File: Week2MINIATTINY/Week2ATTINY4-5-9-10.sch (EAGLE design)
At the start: 16 parts

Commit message: schemematic updates
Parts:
- added R5: (no value), rcl:R-EU_R0603
- JP1: value M021X02_NO_SILK -> RESET_PULLUP_ENABLE
- JP2: value M021X02_NO_SILK -> EXTERNAL_CLK_ENABLE
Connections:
- new net IO1: JP6.2, R1.2
- new net IO2: JP6.3, R2.2
- new net IO3: JP6.4, R3.2
- new net IO4: JP6.5, R4.2
- new net RESET_PULLUP: JP1.2, R5.1
- net GND: now also C1.2, C2.2, C3.2, C4.2, JP6.6
- net PB0: now also R1.1
- net PB1: now also R2.1
- net PB2: now also R3.1
- net PB3/_RESET: now also JP1.1, R4.1
- net VCC: now also C1.1, C2.1, C3.1, C4.1, JP6.1, R5.2
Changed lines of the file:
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@@
 <part name="GND1" library="supply1" library_urn="urn:adsk.eagle:library:371" deviceset="GND" device=""/>
 <part name="P+1" library="supply1" library_urn="urn:adsk.eagle:library:371" deviceset="VCC" device=""/>
-<part name="JP1" library="SparkFun-Connectors" deviceset="M02" device="1X02_NO_SILK"/>
-<part name="JP2" library="SparkFun-Connectors" deviceset="M02" device="1X02_NO_SILK"/>
+<part name="JP1" library="SparkFun-Connectors" deviceset="M02" device="1X02_NO_SILK" value="RESET_PULLUP_ENABLE"/>
+<part name="JP2" library="SparkFun-Connectors" deviceset="M02" device="1X02_NO_SILK" value="EXTERNAL_CLK_ENABLE"/>
 <part name="JP3" library="SparkFun-Connectors" deviceset="M02" device="1X02_NO_SILK"/>
 <part name="JP4" library="SparkFun-Connectors" deviceset="M02" device="1X02_NO_SILK"/>
@@
 <part name="C4" library="rcl" library_urn="urn:adsk.eagle:library:334" deviceset="C-EU" device="C0603K" package3d_urn="urn:adsk.eagle:package:23680/2"/>
 <part name="R4" library="rcl" library_urn="urn:adsk.eagle:library:334" deviceset="R-EU_" device="R0603" package3d_urn="urn:adsk.eagle:package:23555/2"/>
+<part name="GND2" library="supply1" library_urn="urn:adsk.eagle:library:371" deviceset="GND" device=""/>
+<part name="GND3" library="supply1" library_urn="urn:adsk.eagle:library:371" deviceset="GND" device=""/>
+<part name="GND4" library="supply1" library_urn="urn:adsk.eagle:library:371" deviceset="GND" device=""/>
+<part name="GND5" library="supply1" library_urn="urn:adsk.eagle:library:371" deviceset="GND" device=""/>
+<part name="P+2" library="supply1" library_urn="urn:adsk.eagle:library:371" deviceset="VCC" device=""/>
+<part name="P+3" library="supply1" library_urn="urn:adsk.eagle:library:371" deviceset="VCC" device=""/>
+<part name="P+4" library="supply1" library_urn="urn:adsk.eagle:library:371" deviceset="VCC" device=""/>
+<part name="P+5" library="supply1" library_urn="urn:adsk.eagle:library:371" deviceset="VCC" device=""/>
+<part name="R5" library="rcl" library_urn="urn:adsk.eagle:library:334" deviceset="R-EU_" device="R0603" package3d_urn="urn:adsk.eagle:package:23555/2"/>
+<part name="P+6" library="supply1" library_urn="urn:adsk.eagle:library:371" deviceset="VCC" device=""/>
+<part name="P+7" library="supply1" library_urn="urn:adsk.eagle:library:371" deviceset="VCC" device=""/>
+<part name="GND6" library="supply1" library_urn="urn:adsk.eagle:library:371" deviceset="GND" device=""/>
 </parts>
 <sheets>
@@
 <instance part="C4" gate="G$1" x="127" y="38.1"/>
 <instance part="R4" gate="G$1" x="76.2" y="20.32"/>
+<instance part="GND2" gate="1" x="101.6" y="22.86"/>
+<instance part="GND3" gate="1" x="111.76" y="22.86"/>
+<instance part="GND4" gate="1" x="119.38" y="22.86"/>
+<instance part="GND5" gate="1" x="127" y="22.86"/>
+<instance part="P+2" gate="VCC" x="101.6" y="53.34"/>
+<instance part="P+3" gate="VCC" x="111.76" y="53.34"/>
+<instance part="P+4" gate="VCC" x="119.38" y="53.34"/>
+<instance part="P+5" gate="VCC" x="127" y="53.34"/>
+<instance part="R5" gate="G$1" x="71.12" y="63.5" rot="R90"/>
+<instance part="P+6" gate="VCC" x="71.12" y="78.74"/>
+<instance part="P+7" gate="VCC" x="25.4" y="86.36"/>
+<instance part="GND6" gate="1" x="25.4" y="55.88"/>
 </instances>
 <busses>
@@
 <label x="292.1" y="175.26" size="1.778" layer="95"/>
 </segment>
+<segment>
+<pinref part="R4" gate="G$1" pin="1"/>
+<wire x1="71.12" y1="20.32" x2="60.96" y2="20.32" width="0.1524" layer="91"/>
+<label x="58.42" y="20.32" size="1.778" layer="95"/>
+</segment>
+<segment>
+<pinref part="JP1" gate="G$1" pin="1"/>
+<wire x1="165.1" y1="88.9" x2="147.32" y2="88.9" width="0.1524" layer="91"/>
+<label x="147.32" y="88.9" size="1.778" layer="95"/>
+</segment>
 </net>
 <net name="PB2" class="0">
@@
 <label x="292.1" y="170.18" size="1.778" layer="95"/>
 </segment>
+<segment>
+<pinref part="R3" gate="G$1" pin="1"/>
+<wire x1="71.12" y1="27.94" x2="60.96" y2="27.94" width="0.1524" layer="91"/>
+<label x="60.96" y="27.94" size="1.778" layer="95"/>
+</segment>
 </net>
 <net name="PB0" class="0">
@@
 <label x="241.3" y="170.18" size="1.778" layer="95"/>
 </segment>
+<segment>
+<pinref part="R1" gate="G$1" pin="1"/>
+<wire x1="71.12" y1="43.18" x2="60.96" y2="43.18" width="0.1524" layer="91"/>
+<label x="60.96" y="43.18" size="1.778" layer="95"/>
+</segment>
 </net>
 <net name="PB1" class="0">
@@
 <wire x1="251.46" y1="165.1" x2="241.3" y2="165.1" width="0.1524" layer="91"/>
 <label x="241.3" y="165.1" size="1.778" layer="95"/>
+</segment>
+<segment>
+<pinref part="R2" gate="G$1" pin="1"/>
+<wire x1="71.12" y1="35.56" x2="60.96" y2="35.56" width="0.1524" layer="91"/>
+<label x="60.96" y="35.56" size="1.778" layer="95"/>
 </segment>
 </net>
@@
 <pinref part="GND1" gate="1" pin="GND"/>
 </segment>
+<segment>
+<pinref part="C1" gate="G$1" pin="2"/>
+<wire x1="101.6" y1="33.02" x2="101.6" y2="25.4" width="0.1524" layer="91"/>
+<pinref part="GND2" gate="1" pin="GND"/>
+</segment>
+<segment>
+<pinref part="C2" gate="G$1" pin="2"/>
+<wire x1="111.76" y1="33.02" x2="111.76" y2="25.4" width="0.1524" layer="91"/>
+<pinref part="GND3" gate="1" pin="GND"/>
+</segment>
+<segment>
+<pinref part="C3" gate="G$1" pin="2"/>
+<wire x1="119.38" y1="33.02" x2="119.38" y2="25.4" width="0.1524" layer="91"/>
+<pinref part="GND4" gate="1" pin="GND"/>
+</segment>
+<segment>
+<pinref part="C4" gate="G$1" pin="2"/>
+<wire x1="127" y1="33.02" x2="127" y2="25.4" width="0.1524" layer="91"/>
+<pinref part="GND5" gate="1" pin="GND"/>
+</segment>
+<segment>
+<pinref part="JP6" gate="G$1" pin="6"/>
+<wire x1="35.56" y1="63.5" x2="25.4" y2="63.5" width="0.1524" layer="91"/>
+<wire x1="25.4" y1="63.5" x2="25.4" y2="58.42" width="0.1524" layer="91"/>
+<pinref part="GND6" gate="1" pin="GND"/>
+</segment>
 </net>
 <net name="VCC" class="0">
@@
 <pinref part="P+1" gate="VCC" pin="VCC"/>
 </segment>
-</net>
+<segment>
+<pinref part="C1" gate="G$1" pin="1"/>
+<wire x1="101.6" y1="40.64" x2="101.6" y2="50.8" width="0.1524" layer="91"/>
+<pinref part="P+2" gate="VCC" pin="VCC"/>
+</segment>
+<segment>
+<pinref part="C2" gate="G$1" pin="1"/>
+<wire x1="111.76" y1="40.64" x2="111.76" y2="50.8" width="0.1524" layer="91"/>
+<pinref part="P+3" gate="VCC" pin="VCC"/>
+</segment>
+<segment>
+<pinref part="C3" gate="G$1" pin="1"/>
+<wire x1="119.38" y1="40.64" x2="119.38" y2="50.8" width="0.1524" layer="91"/>
+<pinref part="P+4" gate="VCC" pin="VCC"/>
+</segment>
+<segment>
+<pinref part="C4" gate="G$1" pin="1"/>
+<wire x1="127" y1="40.64" x2="127" y2="50.8" width="0.1524" layer="91"/>
+<pinref part="P+5" gate="VCC" pin="VCC"/>
+</segment>
+<segment>
+<pinref part="R5" gate="G$1" pin="2"/>
+<pinref part="P+6" gate="VCC" pin="VCC"/>
+<wire x1="71.12" y1="68.58" x2="71.12" y2="76.2" width="0.1524" layer="91"/>
+</segment>
+<segment>
+<pinref part="JP6" gate="G$1" pin="1"/>
+<wire x1="35.56" y1="76.2" x2="25.4" y2="76.2" width="0.1524" layer="91"/>
+<wire x1="25.4" y1="76.2" x2="25.4" y2="83.82" width="0.1524" layer="91"/>
+<pinref part="P+7" gate="VCC" pin="VCC"/>
+</segment>
+</net>
+<net name="IO1" class="0">
+<segment>
+<pinref part="R1" gate="G$1" pin="2"/>
+<wire x1="81.28" y1="43.18" x2="91.44" y2="43.18" width="0.1524" layer="91"/>
+<label x="88.9" y="43.18" size="1.778" layer="95"/>
+</segment>
+<segment>
+<pinref part="JP6" gate="G$1" pin="2"/>
+<wire x1="35.56" y1="73.66" x2="25.4" y2="73.66" width="0.1524" layer="91"/>
+<label x="25.4" y="73.66" size="1.778" layer="95"/>
+</segment>
+</net>
+<net name="IO2" class="0">
+<segment>
+<pinref part="R2" gate="G$1" pin="2"/>
+<wire x1="81.28" y1="35.56" x2="91.44" y2="35.56" width="0.1524" layer="91"/>
+<label x="88.9" y="35.56" size="1.778" layer="95"/>
+</segment>
+<segment>
+<pinref part="JP6" gate="G$1" pin="3"/>
+<wire x1="35.56" y1="71.12" x2="25.4" y2="71.12" width="0.1524" layer="91"/>
+<label x="25.4" y="71.12" size="1.778" layer="95"/>
+</segment>
+</net>
+<net name="IO3" class="0">
+<segment>
+<pinref part="R3" gate="G$1" pin="2"/>
+<wire x1="81.28" y1="27.94" x2="91.44" y2="27.94" width="0.1524" layer="91"/>
+<label x="88.9" y="27.94" size="1.778" layer="95"/>
+</segment>
+<segment>
+<pinref part="JP6" gate="G$1" pin="4"/>
+<wire x1="35.56" y1="68.58" x2="25.4" y2="68.58" width="0.1524" layer="91"/>
+<label x="25.4" y="68.58" size="1.778" layer="95"/>
+</segment>
+</net>
+<net name="IO4" class="0">
+<segment>
+<pinref part="R4" gate="G$1" pin="2"/>
+<wire x1="81.28" y1="20.32" x2="91.44" y2="20.32" width="0.1524" layer="91"/>
+<label x="88.9" y="20.32" size="1.778" layer="95"/>
+</segment>
+<segment>
+<pinref part="JP6" gate="G$1" pin="5"/>
+<wire x1="35.56" y1="66.04" x2="25.4" y2="66.04" width="0.1524" layer="91"/>
+<label x="25.4" y="66.04" size="1.778" layer="95"/>
+</segment>
+</net>
+<net name="RESET_PULLUP" class="0">
+<segment>
+<pinref part="JP1" gate="G$1" pin="2"/>
+<wire x1="165.1" y1="86.36" x2="147.32" y2="86.36" width="0.1524" layer="91"/>
+<label x="147.32" y="86.36" size="1.778" layer="95"/>
+</segment>
+<segment>
+<pinref part="R5" gate="G$1" pin="1"/>
+<wire x1="71.12" y1="58.42" x2="71.12" y2="50.8" width="0.1524" layer="91"/>
+<label x="71.12" y="50.8" size="1.778" layer="95"/>
+</segment>
+</net>

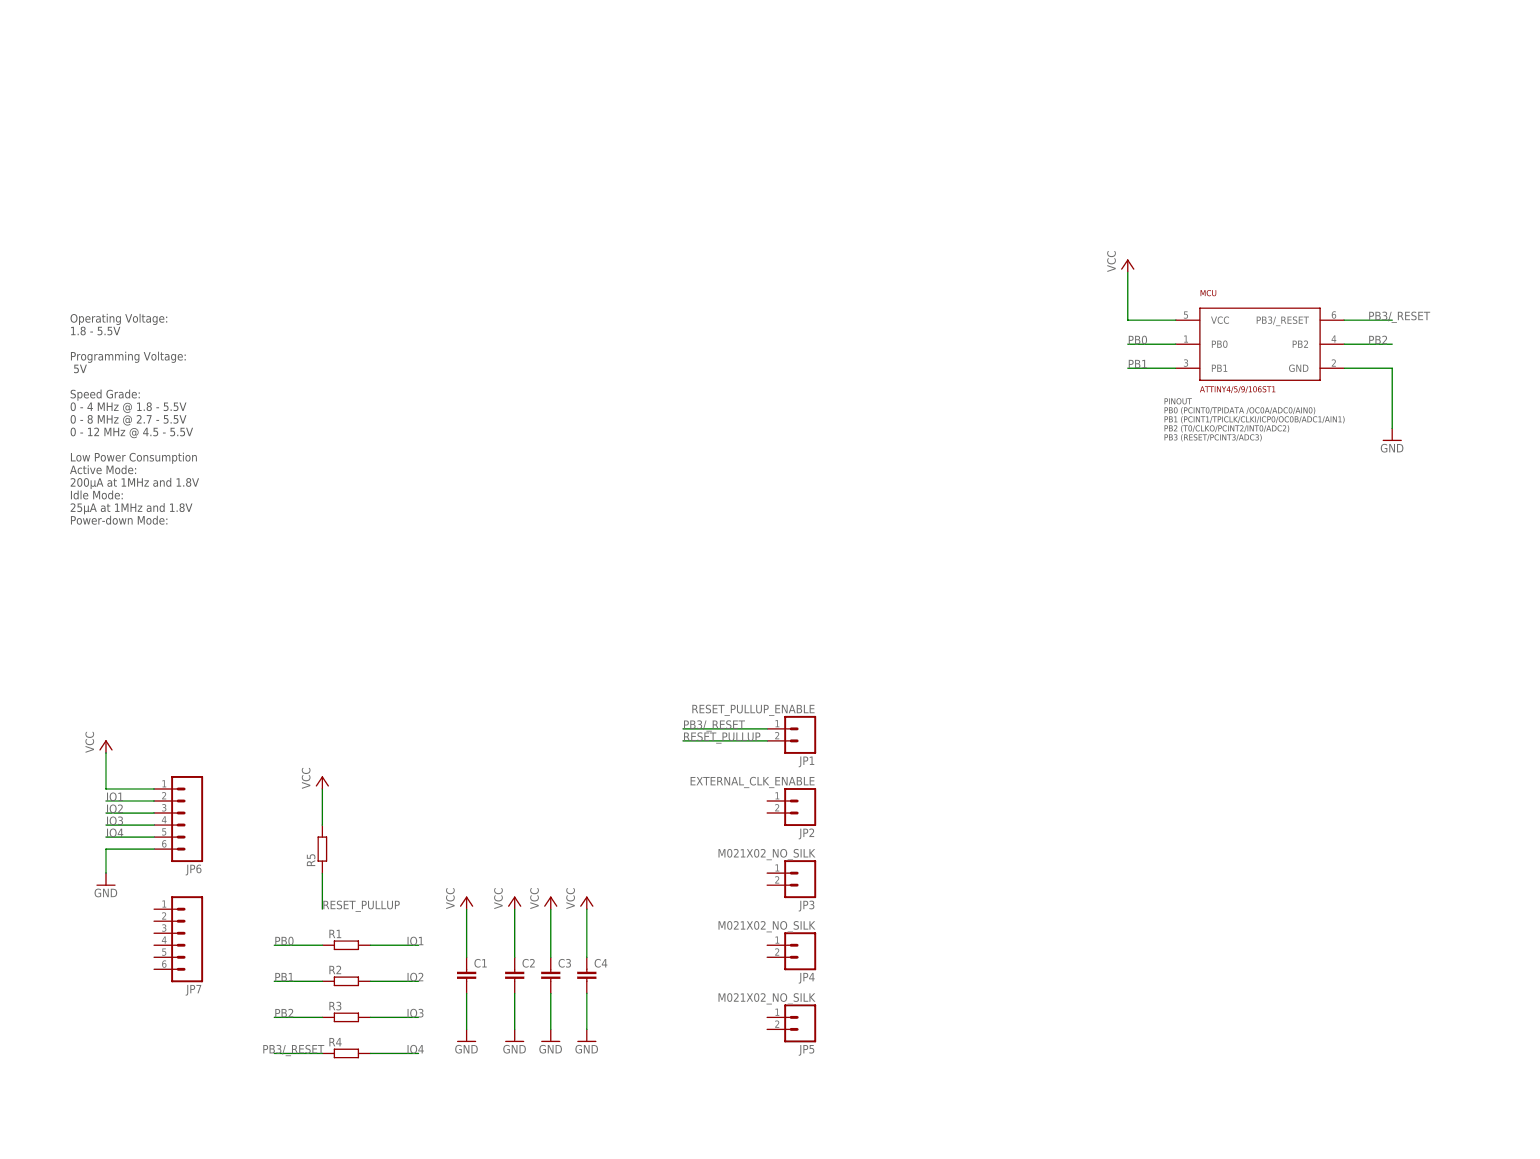
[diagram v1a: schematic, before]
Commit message: started processing gerber for week1 more schmatic work for week 2
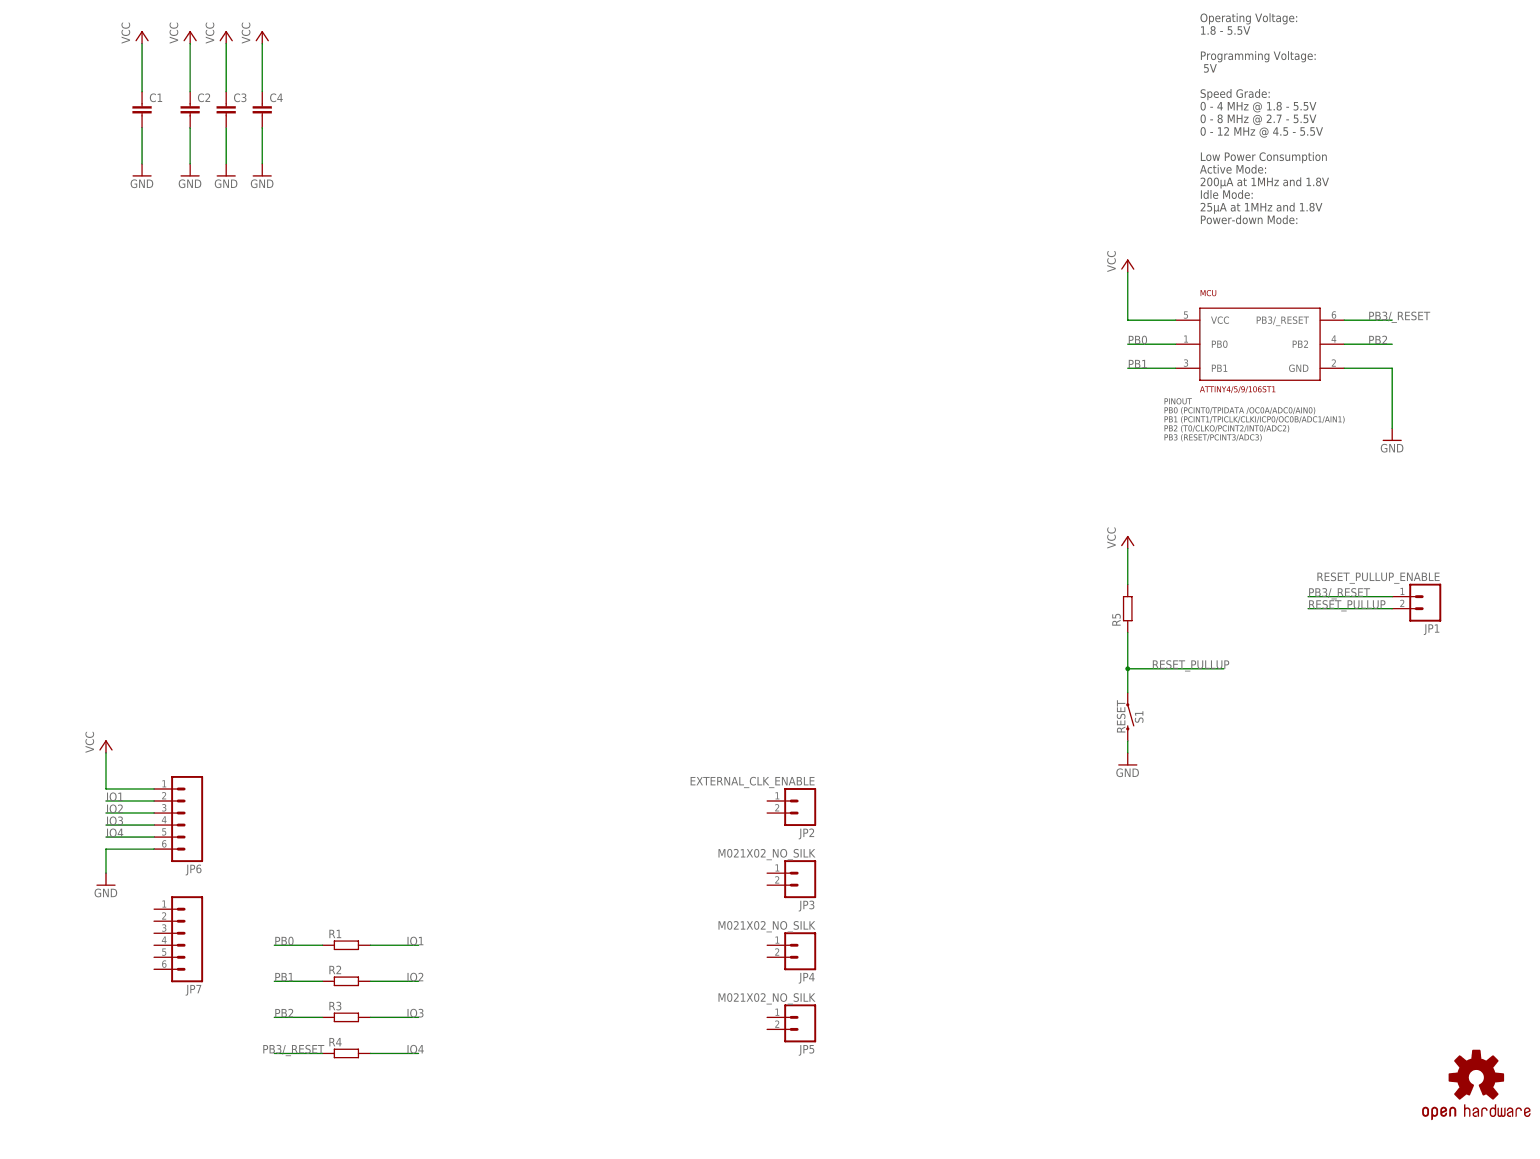
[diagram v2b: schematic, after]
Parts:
- added LOGO1: OSHW-LOGOMINI, SparkFun-Aesthetics:OSHW-LOGOMINI
- added S1: RESET, SparkFun-Switches:MOMENTARY-SWITCH-SPST-PTH-6.0MM
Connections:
- net GND: now also S1.2
- net RESET_PULLUP: now also S1.1
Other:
- moved on the sheet: C1, C2, C3, C4, JP1, R5

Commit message: Week2 schmatics finished started Week3
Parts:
- removed C3, C4: (no value), rcl:C-EUC0603K
- added LED1: Power, led:LEDCHIPLED_0805
- added LED2, LED3, LED4, LED5: (no value), led:LEDCHIPLED_0805
- added R10, R6, R7, R8, R9: (no value), rcl:R-EU_R0603
- JP2: value EXTERNAL_CLK_ENABLE -> LED_SEL_1
- JP3: value M021X02_NO_SILK -> LED_SEL_2
- JP4: value M021X02_NO_SILK -> LED_SEL_3
- JP5: value M021X02_NO_SILK -> LED_SEL_4
- JP7: device SparkFun-Connectors:M06NO_SILK -> pinhead:PINHD-1X5
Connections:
- new net IOLED1: JP2.2, R7.2
- new net IOLED2: JP3.2, R8.2
- new net IOLED3: JP4.2, R9.2
- new net IOLED4: JP5.2, R10.2
- new net N$1: LED1.A, R6.1
- new net N$2: LED2.A, R7.1
- new net N$3: LED3.A, R8.1
- new net N$4: LED4.A, R9.1
- new net N$5: LED5.A, R10.1
- net GND: now also JP7.5, LED1.C, LED2.C, LED3.C, LED4.C, LED5.C; no longer C3.2, C4.2
- net PB0: now also JP2.1, JP7.3
- net PB1: now also JP3.1, JP7.4
- net PB2: now also JP4.1
- net PB3/_RESET: now also JP5.1, JP7.2
- net VCC: now also JP7.1, R6.2; no longer C3.1, C4.1
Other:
- moved on the sheet: JP2, JP3, JP4, JP5
